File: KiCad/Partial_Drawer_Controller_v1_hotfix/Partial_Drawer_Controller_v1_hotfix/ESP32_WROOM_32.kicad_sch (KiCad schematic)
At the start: 41 parts, among them Q2 SS8050, Q3 SS8050, Q4 2N7002T-7-F, Q5 2N7002T-7-F, U5 CP2102N-A02-GQFN28R, U6 ESP32-WROOM-32E-N8, X14 USB-Micro

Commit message: chore: updates parts and BOM export for `Partial_Drawer_Controller_v1_hotfix`
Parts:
- C17, C18, C19, C20, C22, C23, C24: path_to_docs (none) -> Passive_Components/Capacitors/MLCC/Samsung_Electro-Mechanics
- D27: path_to_docs (none) -> Semiconductors/Discrete_Semiconductors/Diodes_Rectifiers/Sc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
- Q2, Q3: path_to_docs (none) -> Semiconductors/Discrete_Semiconductors/Transistors/Bipolar_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
- Q4, Q5: OC_MOUSER (none) -> 621-2N7002T-F; path_to_docs (none) -> Semiconductors/Discrete_Semiconductors/Transistors/MOSFETs/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
- R29, R30, R31, R32, R33, R34, R35, R36, R37, R38, R39, R40, R41, R42, R43, R44, R45, R46: path_to_docs (none) -> Passive_Components/Resistors/UNI-ROYAL
- U5: OC_MOUSER (none) -> 634-CP2102NA02QFN28R; path_to_docs (none) -> Semiconductors/Interface_ICs/USB/Silicon_Labs
- U6: OC_MOUSER (none) -> 356-ESP32WRM32E164PH; path_to_docs (none) -> Embedded_Solutions/Wireless_RF_Modules/ESP32-WROOM-32E-N8
- X14: OC_MOUSER (none) -> 649-10118194-0001LF; path_to_docs (none) -> Connectors/USB/Micro/Amphenol

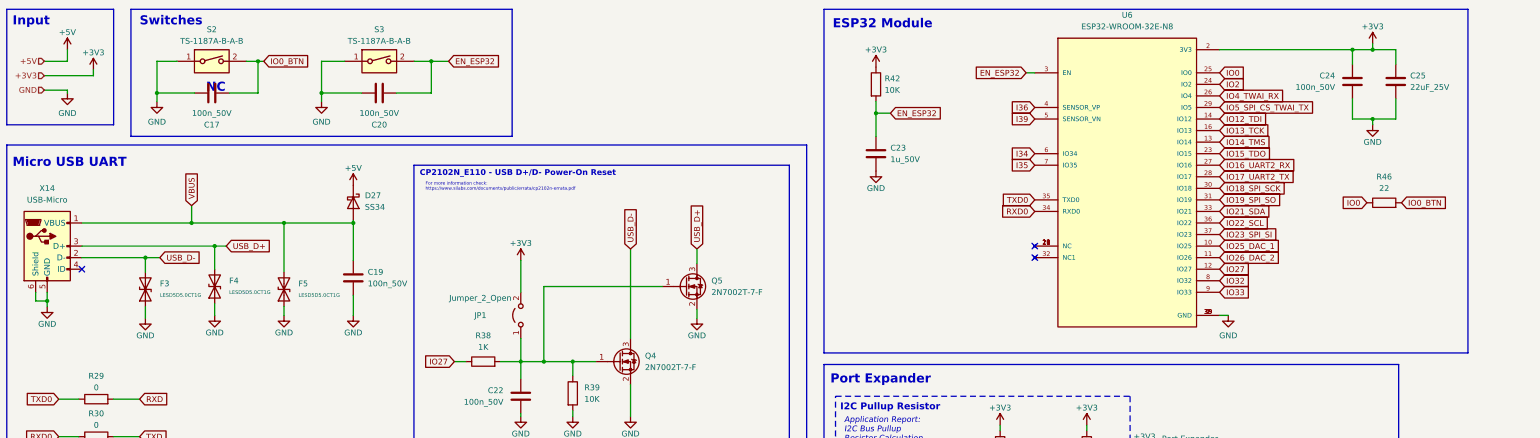
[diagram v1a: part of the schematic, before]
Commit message: chore: updates symbols for `Partial_Drawer_Controller_v1_hotfix` to get docs for every part (not finished yet)
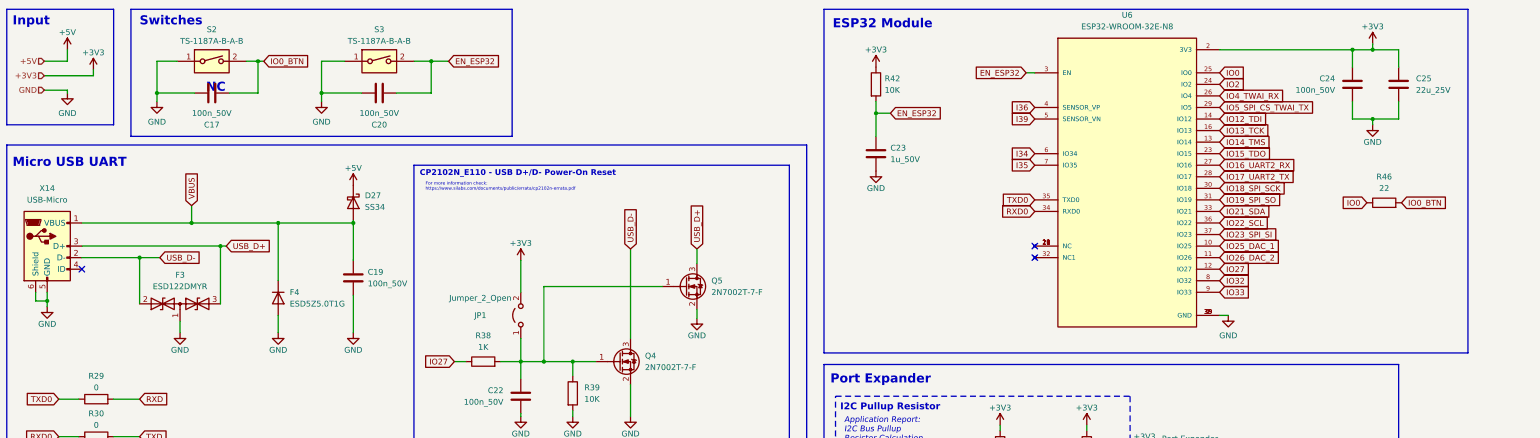
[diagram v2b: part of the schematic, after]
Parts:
- removed C25: 22uF_25V, Capacitor_SMD:C_1206_3216Metric, symbol _C_1206:22uF_25V
- removed F3, F4, F5: LESD5D5.0CT1G, Diode_SMD:D_SOD-523, symbol _Diode_TVS:LESD5D5.0CT1G
- added C25: 22u_25V, Capacitor_SMD:C_1206_3216Metric, symbol _C_1206:22u_25V
- added F3: ESD122DMYR, Robast:Texas_X2SON_DMY0003A, symbol _Diode_TVS:ESD122DMYR
- added F4: ESD5Z5.0T1G, Diode_SMD:D_SOD-523, symbol _Diode_TVS:ESD5Z5.0T1G
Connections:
- net +3V3: now also C25.1
- net GND: now also C25.2, F3.1 (common), F4.2 (A)
- net USB_D+: now also F3.3 (A2)
- net USB_D-: now also F3.2 (A1)
- net VBUS: now also F4.1 (K)
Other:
- moved on the sheet: C24

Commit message: feat: updates `Drawer_Controller_v4_hotfix` and `Partial_Drawer_Controller_v1_hotfix` with newest docs
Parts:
- C21: path_to_docs (none) -> Passive_Components/Capacitors/MLCC/FH
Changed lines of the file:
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@@
 			)
 		)
-		(property "Datasheet" "~"
+		(property "Datasheet" "https://www.lcsc.com/datasheet/lcsc_datasheet_2304140030_FH--Guangdong-Fenghua-Advanced-Tech-1206B475K500NT_C29823.pdf"
 			(at 98.425 122.555 0)
 			(effects
@@
 			(at 98.425 122.555 0)
 			(effects
+				(font
+					(size 1.27 1.27)
+				)
+				(hide yes)
+			)
+		)
+		(property "OC_CONRAD" ""
+			(at 98.425 122.555 0)
+			(effects
+				(font
+					(size 1.27 1.27)
+				)
+				(hide yes)
+			)
+		)
+		(property "OC_RS" ""
+			(at 98.425 122.555 0)
+			(effects
+				(font
+					(size 1.27 1.27)
+				)
+				(hide yes)
+			)
+		)
+		(property "path_to_docs" "Passive_Components/Capacitors/MLCC/FH"
+			(at 98.425 122.555 0)
+			(effects

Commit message: feat: updates `Drawer_Controller_v4_hotfix` and `Partial_Drawer_Controller_v1_hotfix` with docs for tactile switch
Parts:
- S2, S3: path_to_docs (none) -> Electromechanical/Switches/Tactile_Switches/TS-1187A-B-A-B
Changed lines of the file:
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@@
+			)
+		)
+		(property "OC_CONRAD" ""
+			(at 95.885 25.4 0)
+			(effects
+				(font
+					(size 1.27 1.27)
+				)
+				(hide yes)
+			)
+		)
+		(property "OC_RS" ""
+			(at 95.885 25.4 0)
+			(effects
+				(font
+					(size 1.27 1.27)
+				)
+				(hide yes)
+			)
+		)
+		(property "path_to_docs" "Electromechanical/Switches/Tactile_Switches/TS-1187A-B-A-B"
+			(at 95.885 25.4 0)
+			(effects
+				(font
+					(size 1.27 1.27)
+				)
+				(hide yes)
 			)
 		)
@@
 			(at 59.055 25.4 0)
 			(effects
+				(font
+					(size 1.27 1.27)
+				)
+				(hide yes)
+			)
+		)
+		(property "OC_CONRAD" ""
+			(at 59.055 25.4 0)
+			(effects
+				(font
+					(size 1.27 1.27)
+				)
+				(hide yes)
+			)
+		)
+		(property "OC_RS" ""
+			(at 59.055 25.4 0)
+			(effects
+				(font
+					(size 1.27 1.27)
+				)
+				(hide yes)
+			)
+		)
+		(property "path_to_docs" "Electromechanical/Switches/Tactile_Switches/TS-1187A-B-A-B"
+			(at 59.055 25.4 0)
+			(effects
